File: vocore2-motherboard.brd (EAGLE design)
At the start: 100 x 100 mm, 93 parts, among them IC1 AP63205, IC2 FE1.1S, IC3 LM3761MF-3.3, IC4 LM3761MF-3.3, IC5 LM3761MF-3.3, IC6 FT232R, IC7 742G17DBV, J1 RJHSE-5381, J2 TE_1775470-8, J3 AMPHENOL_1140084168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

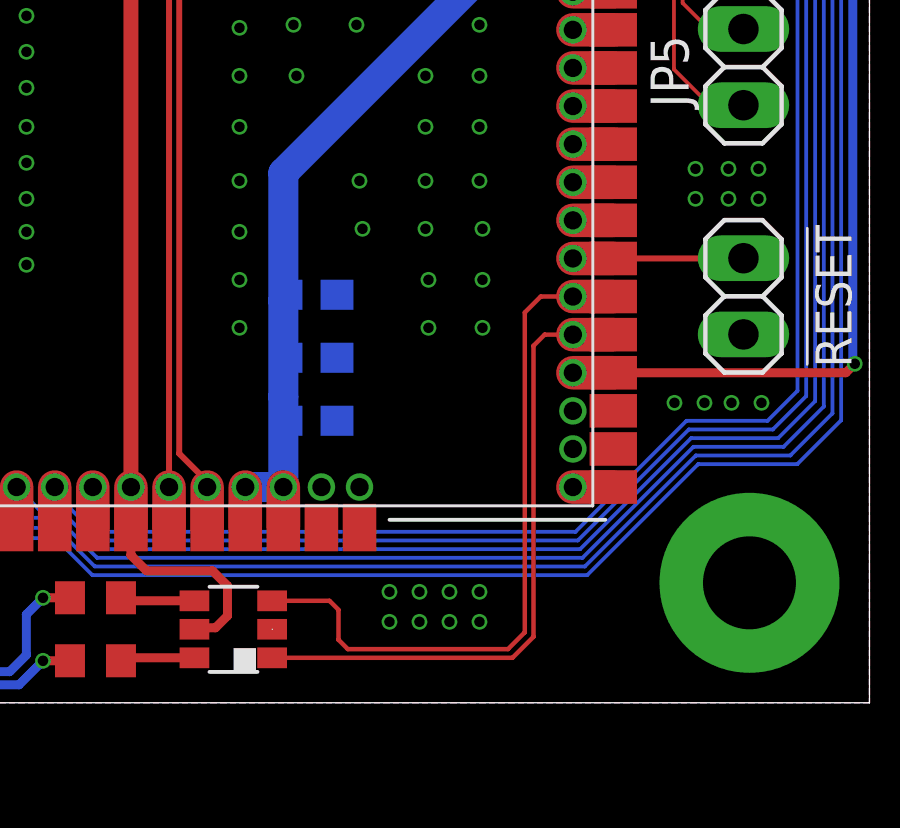
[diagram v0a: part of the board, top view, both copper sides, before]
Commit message: fix: moved LAN_LED_ACT to gpio43
gpio43 can be configured to represent the LNK/ACT state of the Ethernt
PHYs Port 0.
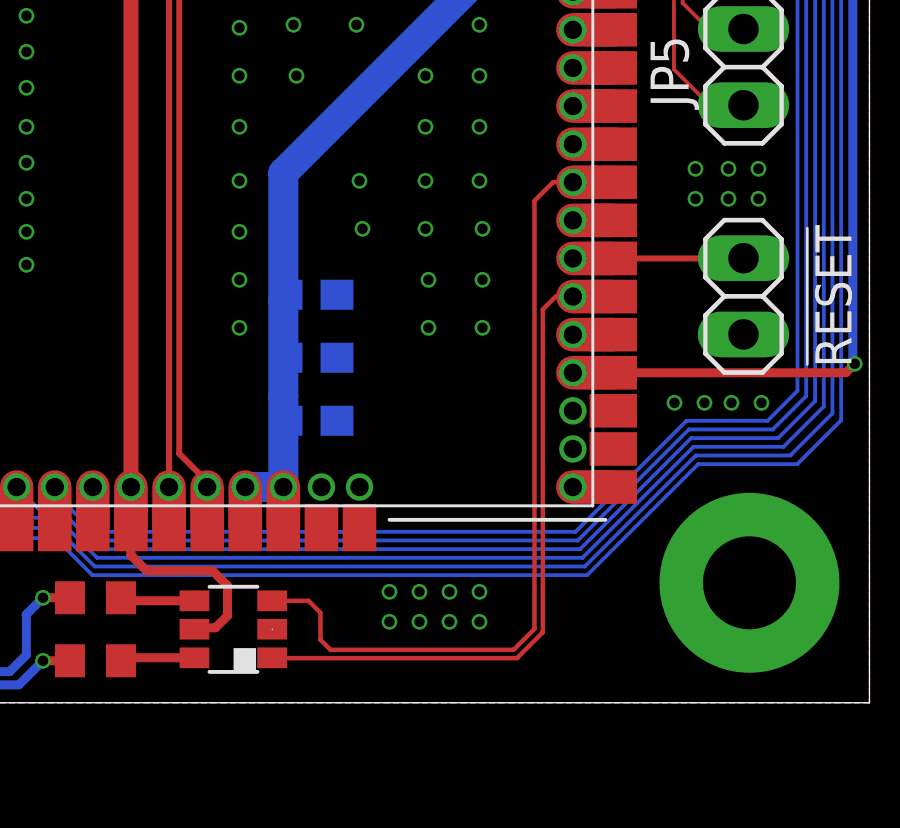
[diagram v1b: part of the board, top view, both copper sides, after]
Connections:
- removed net N$47: U1.143_1, U1.143_2
- new net N$34: U1.136_1, U1.136_2
- net LED_LAN_ACT: now also IC7.3, U1.143_1, U1.143_2; no longer IC7.1, U1.136_1, U1.136_2
- net LED_LAN_LNK: now also IC7.1; no longer IC7.3
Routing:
- net LED_LAN_ACT: track 21.5 -> 27.4 mm
- net N$47: track 1.35 -> 0.00 mm
- net N$34: track 0.00 -> 1.35 mm
- net LED_LAN_LNK: track 23.7 -> 22.7 mm
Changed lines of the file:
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@@
 </signal>
 <signal name="LED_LAN_ACT">
-<contactref element="U1" pad="136_2"/>
-<contactref element="U1" pad="136_1"/>
-<wire x1="41.46" y1="12.272" x2="40.114" y2="12.272" width="1.12" layer="1"/>
-<contactref element="IC7" pad="1"/>
-<wire x1="40.114" y1="12.272" x2="39.172" y2="12.272" width="0.15" layer="1"/>
-<wire x1="39.172" y1="12.272" x2="38.8" y2="11.9" width="0.15" layer="1"/>
-<wire x1="38.8" y1="11.9" x2="38.8" y2="2.2" width="0.15" layer="1"/>
-<wire x1="38.8" y1="2.2" x2="38.1" y2="1.5" width="0.15" layer="1"/>
-<wire x1="38.1" y1="1.5" x2="30.09" y2="1.5" width="0.15" layer="1"/>
+<contactref element="U1" pad="143_1"/>
+<contactref element="U1" pad="143_2"/>
+<wire x1="41.46" y1="17.352" x2="40.114" y2="17.352" width="1.12" layer="1"/>
+<contactref element="IC7" pad="3"/>
+<wire x1="40.114" y1="17.352" x2="39.452" y2="17.352" width="0.15" layer="1"/>
+<wire x1="39.452" y1="17.352" x2="38.8341" y2="16.7341" width="0.15" layer="1"/>
+<wire x1="38.8341" y1="16.7341" x2="38.8341" y2="2.46369375" width="0.15" layer="1"/>
+<wire x1="38.8341" y1="2.46369375" x2="38.13630625" y2="1.7659" width="0.15" layer="1"/>
+<wire x1="32.0341" y1="1.7659" x2="31.7" y2="2.1" width="0.15" layer="1"/>
+<wire x1="31.7" y1="2.1" x2="31.7" y2="3" width="0.15" layer="1"/>
+<wire x1="31.7" y1="3" x2="31.3" y2="3.4" width="0.15" layer="1"/>
+<wire x1="31.3" y1="3.4" x2="30.09" y2="3.4" width="0.15" layer="1"/>
+<wire x1="38.13630625" y1="1.7659" x2="32.0341" y2="1.7659" width="0.15" layer="1"/>
 </signal>
 <signal name="LED_LAN_LNK">
@@
 <contactref element="U1" pad="137_1"/>
 <wire x1="41.46" y1="13.542" x2="40.114" y2="13.542" width="1.12" layer="1"/>
-<contactref element="IC7" pad="3"/>
-<wire x1="40.114" y1="13.542" x2="39.042" y2="13.542" width="0.15" layer="1"/>
-<wire x1="39.042" y1="13.542" x2="38.5111" y2="13.0111" width="0.15" layer="1"/>
-<wire x1="38.5111" y1="13.0111" x2="38.5111" y2="2.34895625" width="0.15" layer="1"/>
-<wire x1="38.5111" y1="2.34895625" x2="37.95104375" y2="1.7889" width="0.15" layer="1"/>
-<wire x1="32.6111" y1="1.7889" x2="32.3" y2="2.1" width="0.15" layer="1"/>
-<wire x1="37.95104375" y1="1.7889" x2="32.6111" y2="1.7889" width="0.15" layer="1"/>
-<wire x1="32.3" y1="3.1" x2="32.3" y2="2.1" width="0.15" layer="1"/>
-<wire x1="30.09" y1="3.4" x2="32" y2="3.4" width="0.15" layer="1"/>
-<wire x1="32" y1="3.4" x2="32.3" y2="3.1" width="0.15" layer="1"/>
+<wire x1="40.114" y1="13.542" x2="39.542" y2="13.542" width="0.15" layer="1"/>
+<wire x1="39.542" y1="13.542" x2="39.1111" y2="13.1111" width="0.15" layer="1"/>
+<wire x1="39.1111" y1="13.1111" x2="39.1111" y2="2.34895625" width="0.15" layer="1"/>
+<wire x1="39.1111" y1="2.34895625" x2="38.25104375" y2="1.4889" width="0.15" layer="1"/>
+<contactref element="IC7" pad="1"/>
+<wire x1="30.1011" y1="1.4889" x2="30.09" y2="1.5" width="0.15" layer="1"/>
+<wire x1="38.25104375" y1="1.4889" x2="30.1011" y2="1.4889" width="0.15" layer="1"/>
 </signal>
 <signal name="N$43">
@@
 <contactref element="U1" pad="142_1"/>
 <wire x1="41.46" y1="16.082" x2="40.114" y2="16.082" width="1.12" layer="1"/>
-</signal>
-<signal name="N$47">
-<contactref element="U1" pad="143_1"/>
-<contactref element="U1" pad="143_2"/>
-<wire x1="41.46" y1="17.352" x2="40.114" y2="17.352" width="1.12" layer="1"/>
 </signal>
 <signal name="N$49">
@@
 <wire x1="-34.90856875" y1="31.1" x2="-33.61966875" y2="29.8111" width="0.3" layer="1"/>
 </signal>
+<signal name="N$34">
+<contactref element="U1" pad="136_2"/>
+<contactref element="U1" pad="136_1"/>
+<wire x1="40.114" y1="12.272" x2="41.46" y2="12.272" width="1.12" layer="1"/>
+</signal>
 </signals>

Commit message: fix: typo in partname LM3761MF -> LM3671MF
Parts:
- IC3, IC4, IC5: value LM3761MF-3.3 -> LM3671MF-3.3
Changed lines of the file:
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@@
 <attribute name="SPICEPREFIX" value="R" x="-51.9" y="7.8" size="1.778" layer="27" rot="R90" display="off"/>
 </element>
-<element name="IC4" library="texas" package="SOT95P284X122-5N" value="LM3761MF-3.3" x="23.5" y="60.35" smashed="yes" rot="R270">
+<element name="IC4" library="texas" package="SOT95P284X122-5N" value="LM3671MF-3.3" x="23.5" y="60.35" smashed="yes" rot="R270">
 <attribute name="FARNELL" value="1685767" x="23.5" y="60.35" size="1.778" layer="27" rot="R270" display="off"/>
 <attribute name="MBM" value="1" x="23.5" y="60.35" size="1.778" layer="27" rot="R270" display="off"/>
@@
 <attribute name="PREIS" value="1,70" x="23.5" y="46.65" size="1.778" layer="27" display="off"/>
 </element>
-<element name="IC3" library="texas" package="SOT95P284X122-5N" value="LM3761MF-3.3" x="-10.05" y="60.35" smashed="yes" rot="R270">
+<element name="IC3" library="texas" package="SOT95P284X122-5N" value="LM3671MF-3.3" x="-10.05" y="60.35" smashed="yes" rot="R270">
 <attribute name="FARNELL" value="1685767" x="-10.05" y="60.35" size="1.778" layer="27" rot="R270" display="off"/>
 <attribute name="MBM" value="1" x="-10.05" y="60.35" size="1.778" layer="27" rot="R270" display="off"/>
@@
 <attribute name="PREIS" value="1,70" x="-10.05" y="46.65" size="1.778" layer="27" display="off"/>
 </element>
-<element name="IC5" library="texas" package="SOT95P284X122-5N" value="LM3761MF-3.3" x="-43.55" y="60.35" smashed="yes" rot="R270">
+<element name="IC5" library="texas" package="SOT95P284X122-5N" value="LM3671MF-3.3" x="-43.55" y="60.35" smashed="yes" rot="R270">
 <attribute name="FARNELL" value="1685767" x="-43.55" y="60.35" size="1.778" layer="27" rot="R270" display="off"/>
 <attribute name="MBM" value="1" x="-43.55" y="60.35" size="1.778" layer="27" rot="R270" display="off"/>

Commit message: feat: added digikey part numbers
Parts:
- R12, R13, R8, R9: value (none) -> 75R

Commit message: fix: proper colors for leds
PWR = red
MPCIE_PWR = orange
MPCIE_USB = green
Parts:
- LED1, LED2, LED4: value GREEN -> ORANGE
- LED3: value GREEN -> RED
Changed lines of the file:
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@@
 <attribute name="SPICEPREFIX" value="C" x="3.9" y="71.5" size="1.778" layer="27" rot="R180" display="off"/>
 </element>
-<element name="LED3" library="led" library_urn="urn:adsk.eagle:library:259" package="CHIP-LED0805" package3d_urn="urn:adsk.eagle:package:15818/2" value="GREEN" x="-46" y="14" smashed="yes">
+<element name="LED3" library="led" library_urn="urn:adsk.eagle:library:259" package="CHIP-LED0805" package3d_urn="urn:adsk.eagle:package:15818/2" value="RED" x="-46" y="14" smashed="yes">
 <attribute name="FARNELL" value="1686076" x="-52.2" y="21.5" size="1.778" layer="27" display="off"/>
 <attribute name="MBM" value="5" x="-52.2" y="21.5" size="1.778" layer="27" display="off"/>
@@
 <attribute name="FARNELL" value="2457514" x="-43.55" y="46.65" size="1.778" layer="27" display="off"/>
 </element>
-<element name="LED1" library="led" library_urn="urn:adsk.eagle:library:259" package="CHIP-LED0805" package3d_urn="urn:adsk.eagle:package:15818/2" value="GREEN" x="44.3" y="39.6" smashed="yes">
+<element name="LED1" library="led" library_urn="urn:adsk.eagle:library:259" package="CHIP-LED0805" package3d_urn="urn:adsk.eagle:package:15818/2" value="ORANGE" x="44.3" y="39.6" smashed="yes">
 <attribute name="FARNELL" value="1686076" x="38.1" y="47.1" size="1.778" layer="27" display="off"/>
 <attribute name="MBM" value="5" x="38.1" y="47.1" size="1.778" layer="27" display="off"/>
@@
 <attribute name="SPICEPREFIX" value="R" x="51.8" y="33.4" size="1.778" layer="28" rot="MR90" display="off"/>
 </element>
-<element name="LED2" library="led" library_urn="urn:adsk.eagle:library:259" package="CHIP-LED0805" package3d_urn="urn:adsk.eagle:package:15818/2" value="GREEN" x="10.8" y="39.6" smashed="yes">
+<element name="LED2" library="led" library_urn="urn:adsk.eagle:library:259" package="CHIP-LED0805" package3d_urn="urn:adsk.eagle:package:15818/2" value="ORANGE" x="10.8" y="39.6" smashed="yes">
 <attribute name="FARNELL" value="1686076" x="4.6" y="47.1" size="1.778" layer="27" display="off"/>
 <attribute name="MBM" value="5" x="4.6" y="47.1" size="1.778" layer="27" display="off"/>
@@
 <attribute name="SPICEPREFIX" value="R" x="18.3" y="33.4" size="1.778" layer="28" rot="MR90" display="off"/>
 </element>
-<element name="LED4" library="led" library_urn="urn:adsk.eagle:library:259" package="CHIP-LED0805" package3d_urn="urn:adsk.eagle:package:15818/2" value="GREEN" x="-22.7" y="39.6" smashed="yes">
+<element name="LED4" library="led" library_urn="urn:adsk.eagle:library:259" package="CHIP-LED0805" package3d_urn="urn:adsk.eagle:package:15818/2" value="ORANGE" x="-22.7" y="39.6" smashed="yes">
 <attribute name="FARNELL" value="1686076" x="-28.9" y="47.1" size="1.778" layer="27" display="off"/>
 <attribute name="MBM" value="5" x="-28.9" y="47.1" size="1.778" layer="27" display="off"/>

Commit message: fix: corrected led restistor values
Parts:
- R10, R2, R4, R5, R6: value 330R -> 150R
- R14, R15: value 330R -> 820R

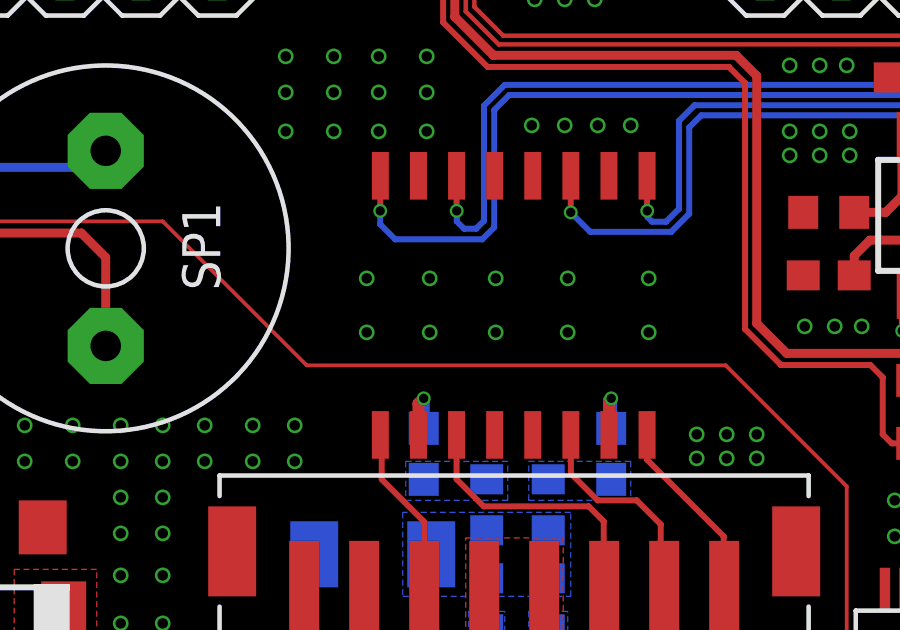
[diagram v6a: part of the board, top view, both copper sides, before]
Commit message: refactor: new symbol for ethernet transformer U4
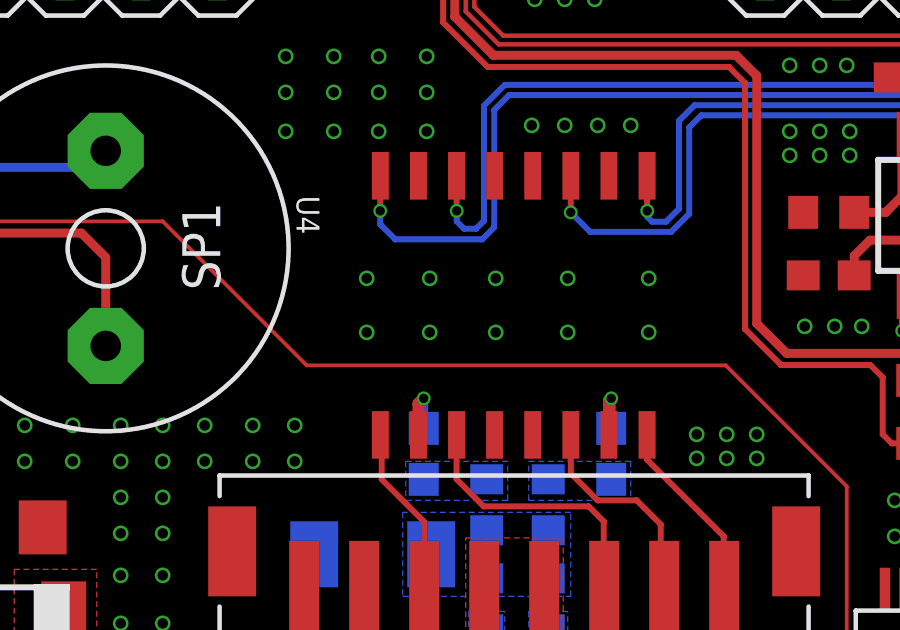
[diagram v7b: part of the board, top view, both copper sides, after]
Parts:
- renumbered U3 to U4
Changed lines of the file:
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@@
 <layer number="25" name="tNames" color="7" fill="1" visible="yes" active="yes"/>
 <layer number="26" name="bNames" color="7" fill="1" visible="yes" active="yes"/>
-<layer number="27" name="tValues" color="7" fill="1" visible="yes" active="yes"/>
+<layer number="27" name="tValues" color="7" fill="1" visible="no" active="yes"/>
 <layer number="28" name="bValues" color="7" fill="1" visible="yes" active="yes"/>
 <layer number="29" name="tStop" color="7" fill="3" visible="no" active="yes"/>
@@
 <attribute name="VALUE" x="48.975" y="19.92" size="1.27" layer="27" rot="R90"/>
 </element>
-<element name="U3" library="ethernet-transformer" package="S558-5999-U7-F" value="S558-5999-U7-F" x="-16" y="27.4" smashed="yes" rot="R270">
-<attribute name="DIGIKEY" value="507-1463-1-ND" x="-16" y="27.4" size="1.778" layer="27" rot="R270" display="off"/>
-<attribute name="MANUFACTURER_PART_NUMBER" value="S5585999U7F" x="-16" y="27.4" size="1.778" layer="27" rot="R270" display="off"/>
-<attribute name="VENDOR" value="Belfuse" x="-16" y="27.4" size="1.778" layer="27" rot="R270" display="off"/>
-</element>
 <element name="J1" library="RJHSE-5381" package="AMPHENOL_RJHSE-5381" value="RJHSE-5381" x="-16" y="3.4" smashed="yes">
 <attribute name="DESCRIPTION" value=" connector, mod jack, rt angle pcb, shielded, led1-g, led2-y, single port, rj-45 8 cont " x="-16" y="3.4" size="1.778" layer="27" display="off"/>
@@
 <attribute name="DIGIKEY" value="BSS123LT1GOSCT-ND‎" x="-38.6" y="31.1" size="1.778" layer="27" rot="R270" display="off"/>
 </element>
+<element name="U4" library="ethernet-transformer" package="S558-5999-U7-F" value="S558-5999-U7-F" x="-16" y="27.4" smashed="yes" rot="R270">
+<attribute name="DIGIKEY" value="507-1463-1-ND" x="-16" y="27.4" size="1.778" layer="27" rot="R270" display="off"/>
+<attribute name="NAME" x="-23.239" y="31.0576" size="0.762" layer="25" ratio="6" rot="SR270"/>
+</element>
 </elements>
 <signals>
@@
 <contactref element="J2" pad="7"/>
 <contactref element="J2" pad="8"/>
-<contactref element="C23" pad="2"/>
 <contactref element="C24" pad="1"/>
 <contactref element="C57" pad="2"/>
@@
 <via x="12.6" y="24.8" extent="1-16" drill="0.35"/>
 <via x="12.6" y="26.1" extent="1-16" drill="0.35"/>
+<contactref element="C23" pad="2"/>
 </signal>
 <signal name="N$1">
@@
 <contactref element="U1" pad="33_2"/>
 <wire x1="15.14" y1="23.067" x2="16.492" y2="23.067" width="1.12" layer="1"/>
-<contactref element="U3" pad="6"/>
 <wire x1="16.492" y1="23.067" x2="15.933" y2="23.067" width="0.2" layer="16"/>
 <wire x1="15.933" y1="23.067" x2="15.7" y2="23.3" width="0.2" layer="16"/>
@@
 <wire x1="-17.654284375" y1="29.954284375" x2="-17.9" y2="30.2" width="0.2" layer="16"/>
 <wire x1="-17.9" y1="30.2" x2="-17.9" y2="30.55" width="0.2" layer="16"/>
+<contactref element="U4" pad="6"/>
 </signal>
 <signal name="VOCORE_TXD2">
@@
 <contactref element="U1" pad="34_1"/>
 <wire x1="15.14" y1="21.797" x2="16.492" y2="21.797" width="1.12" layer="1"/>
-<contactref element="U3" pad="8"/>
 <wire x1="16.492" y1="21.797" x2="15.3611" y2="22.9279" width="0.2" layer="16"/>
 <wire x1="15.3611" y1="22.9279" x2="15.3611" y2="32.33033125" width="0.2" layer="16"/>
@@
 <wire x1="-19.95" y1="29.6" x2="-20.45" y2="30.1" width="0.2" layer="16"/>
 <wire x1="-20.45" y1="30.1" x2="-20.45" y2="30.55" width="0.2" layer="16"/>
+<contactref element="U4" pad="8"/>
 </signal>
 <signal name="P0_TD+">
@@
 <contactref element="U1" pad="35_1"/>
 <wire x1="15.14" y1="20.527" x2="16.492" y2="20.527" width="1.12" layer="1"/>
-<contactref element="U3" pad="1"/>
 <wire x1="16.492" y1="20.527" x2="15.0222" y2="21.9968" width="0.2" layer="16"/>
 <wire x1="15.0222" y1="21.9968" x2="15.0222" y2="32.1606625" width="0.2" layer="16"/>
@@
 <wire x1="-10.91966875" y1="30.1889" x2="-10.4889" y2="30.61966875" width="0.2" layer="16"/>
 <wire x1="-11.3889" y1="30.1889" x2="-10.91966875" y2="30.1889" width="0.2" layer="16"/>
+<contactref element="U4" pad="1"/>
 </signal>
 <signal name="P0_TD-">
@@
 <wire x1="15.14" y1="19.247" x2="16.482" y2="19.247" width="1.12" layer="1"/>
 <wire x1="16.482" y1="19.247" x2="16.492" y2="19.257" width="1.12" layer="1"/>
-<contactref element="U3" pad="3"/>
 <wire x1="16.492" y1="19.257" x2="14.6833" y2="21.0657" width="0.2" layer="16"/>
 <wire x1="14.6833" y1="21.0657" x2="14.6833" y2="31.99099375" width="0.2" layer="16"/>
@@
 <wire x1="-14.1" y1="31.713" x2="-14.095" y2="31.718" width="0.2" layer="1"/>
 <wire x1="-10.15" y1="33.3333" x2="-10.15" y2="30.45" width="0.2" layer="16"/>
+<contactref element="U4" pad="3"/>
 </signal>
 <signal name="VC_SPI_MOSI">
@@
 <vertex x="-28.6" y="7.4"/>
 </polygon>
-<contactref element="C22" pad="2"/>
 <via x="-16.9" y="11.95" extent="1-16" drill="0.31"/>
 <via x="-16.9" y="12.6" extent="1-16" drill="0.31"/>
@@
 <vertex x="-17.5" y="14.3"/>
 </polygon>
+<contactref element="C22" pad="2"/>
 </signal>
 <signal name="TX+">
-<contactref element="U3" pad="16"/>
 <contactref element="J1" pad="1"/>
 <contactref element="J2" pad="1"/>
@@
 <wire x1="-11.555" y1="22.255" x2="-9" y2="19.7" width="0.2" layer="1"/>
 <wire x1="-9" y1="19.7" x2="-9" y2="16.785003125" width="0.2" layer="1"/>
+<contactref element="U4" pad="16"/>
 </signal>
 <signal name="TX-">
-<contactref element="U3" pad="14"/>
 <contactref element="J1" pad="2"/>
 <contactref element="J2" pad="2"/>
@@
 <wire x1="-10.985" y1="16.8" x2="-11.1" y2="16.915" width="0.2" layer="1"/>
 <wire x1="-11.1" y1="16.915" x2="-11.1" y2="20.1" width="0.2" layer="1"/>
+<contactref element="U4" pad="14"/>
 </signal>
 <signal name="RX+">
-<contactref element="U3" pad="11"/>
 <contactref element="J1" pad="3"/>
 <contactref element="J2" pad="3"/>
@@
 <wire x1="-13" y1="20.2" x2="-13" y2="16.114996875" width="0.2" layer="1"/>
 <wire x1="-13" y1="16.114996875" x2="-12.985003125" y2="16.1" width="0.2" layer="1"/>
+<contactref element="U4" pad="11"/>
 </signal>
 <signal name="RX-">
-<contactref element="U3" pad="9"/>
 <contactref element="J1" pad="6"/>
 <contactref element="J2" pad="6"/>
@@
 <wire x1="-20.445" y1="23.082" x2="-20.4" y2="23.037" width="0.2" layer="1"/>
 <wire x1="-20.4" y1="23.037" x2="-20.4" y2="21.6" width="0.2" layer="1"/>
+<contactref element="U4" pad="9"/>
 </signal>
 <signal name="N$7">
-<contactref element="U3" pad="15"/>
-<contactref element="C20" pad="2"/>
 <wire x1="-12.825" y1="23.082" x2="-12.825" y2="24.225" width="0.4" layer="1"/>
 <wire x1="-12.825" y1="24.225" x2="-12.75" y2="24.3" width="0.4" layer="1"/>
 <via x="-12.75" y="24.3" extent="1-16" drill="0.31"/>
-<wire x1="-12.75" y1="24.3" x2="-12.75" y2="23.3" width="0.4" layer="16"/>
+<contactref element="U4" pad="15"/>
+<contactref element="C20" pad="2"/>
+<wire x1="-12.75" y1="23.3" x2="-12.75" y2="24.3" width="0.3" layer="16"/>
 </signal>
 <signal name="N$16">
-<contactref element="U3" pad="10"/>
-<contactref element="C21" pad="2"/>
 <wire x1="-19.175" y1="23.082" x2="-19.175" y2="24.125" width="0.4" layer="1"/>
 <wire x1="-19.175" y1="24.125" x2="-19" y2="24.3" width="0.4" layer="1"/>
 <via x="-19" y="24.3" extent="1-16" drill="0.31"/>
-<wire x1="-19" y1="24.3" x2="-19" y2="23.3" width="0.4" layer="16"/>
+<contactref element="U4" pad="10"/>
+<contactref element="C21" pad="2"/>
+<wire x1="-19" y1="23.3" x2="-19" y2="24.3" width="0.3" layer="16"/>
 </signal>
 <signal name="N$17">
@@
 <signal name="N$33">
 <contactref element="R8" pad="2"/>
-<contactref element="R9" pad="2"/>
-<contactref element="R12" pad="2"/>
-<contactref element="R13" pad="2"/>
-<contactref element="C24" pad="2"/>
 <polygon width="0.1" layer="16" thermals="no">
 <vertex x="-19.7" y="17.7"/>
@@
 <vertex x="-19.7" y="20.5"/>
 </polygon>
+<contactref element="R9" pad="2"/>
+<contactref element="R12" pad="2"/>
+<contactref element="R13" pad="2"/>
+<contactref element="C24" pad="2"/>
 </signal>
 <signal name="N$56">
